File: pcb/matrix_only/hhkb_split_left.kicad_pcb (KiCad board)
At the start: 2 copper layers, 138.4 x 97.4 mm, 65 parts, among them SW1 CPG151101S11-2, SW10 CPG151101S11-2, SW11 CPG151101S11-2, SW12 CPG151101S11-2, SW13 CPG151101S11-2, SW14 CPG151101S11-2, SW15 CPG151101S11-2, SW16 CPG151101S11-2, SW17 CPG151101S11-2, SW18 CPG151101S11-2, SW19 CPG151101S11-2, SW2 CPG151101S11-2, SW20 CPG151101S11-2, SW21 CPG151101S11-2, SW22 CPG151101S11-2, SW23 CPG151101S11-2, SW24 CPG151101S11-2, SW25 CPG151101S11-2, SW26 CPG151101S11-2, SW27 CPG151101S11-2, SW3 CPG151101S11-2, SW4 CPG151101S11-2, SW5 CPG151101S11-2, SW6 CPG151101S11-2, SW7 CPG151101S11-2, SW8 CPG151101S11-2, SW9 CPG151101S11-2, U1 74LVC595

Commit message: #19 決着: 右 J_DB を 1.63mm 手前へ（ソケットまで 3.9mm）、左右の配線と露出ビアを利用者が引き直し。3 基板とも DRC 0 / 未配線 0
- 右: MP パッドに当たった COL0 の迂回、V3V3 の裏面残骸 2 本を削除、MOSI ビアを 0.15mm 移動、混んだ V3V3 ビアを φ0.56（アニュラー 0.13）
- gen_pcb: 右 J_DB の dy を +1.235（中心 y=88.46）に
- 検査 458 緑・赤 1（左 SPI_SCK の露出のみ・任意）
- 記録・部品記録・DRC 記録・証拠ページを更新

Co-Authored-By: Claude Fable 5 <noreply@anthropic.com>
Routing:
- net SPARE: track 9.81 -> 14.7 mm
- net SPARE2: track 10.2 -> 13.0 mm
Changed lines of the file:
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@@
 	)
 	(via
-		(at 209.94 75.69)
+		(at 216.34 77.01)
 		(size 0.6)
 		(drill 0.3)
@@
 	)
 	(segment
-		(start 209.93 78.36)
+		(start 209.93 77.32)
 		(end 209.93 83.964314)
+		(width 0.2)
+		(layer "B.Cu")
+		(net "SPARE")
+	)
+	(segment
+		(start 216.34 77.01)
+		(end 210.24 77.01)
 		(width 0.2)
 		(layer "B.Cu")
@@
 	)
 	(segment
-		(start 209.94 75.69)
-		(end 209.94 78.35)
-		(width 0.2)
-		(layer "B.Cu")
-		(net "SPARE")
-	)
-	(segment
-		(start 209.94 78.35)
-		(end 209.93 78.36)
-		(width 0.2)
-		(layer "B.Cu")
-		(net "SPARE")
-	)
-	(segment
 		(start 209.63125 84.263064)
 		(end 209.63125 85.375)
@@
 		(net "SPARE")
 	)
+	(segment
+		(start 210.24 77.01)
+		(end 209.93 77.32)
+		(width 0.2)
+		(layer "B.Cu")
+		(net "SPARE")
+	)
 	(via
-		(at 211.22 75.67)
+		(at 216.36 78.23)
 		(size 0.6)
 		(drill 0.3)
@@
 	)
 	(segment
-		(start 211.22 75.67)
-		(end 210.53 76.36)
-		(width 0.2)
-		(layer "B.Cu")
-		(net "SPARE2")
-	)
-	(segment
 		(start 210.13125 84.32875)
 		(end 210.13125 85.375)
@@
 	)
 	(segment
-		(start 210.53 76.36)
+		(start 216.36 78.23)
+		(end 210.76 78.23)
+		(width 0.2)
+		(layer "B.Cu")
+		(net "SPARE2")
+	)
+	(segment
+		(start 210.53 78.46)
 		(end 210.53 83.93)
 		(width 0.2)
 		(layer "B.Cu")
+		(net "SPARE2")
+	)
+	(segment
+		(start 210.76 78.23)
+		(end 210.53 78.46)
+		(width 0.2)
+		(layer "B.Cu")

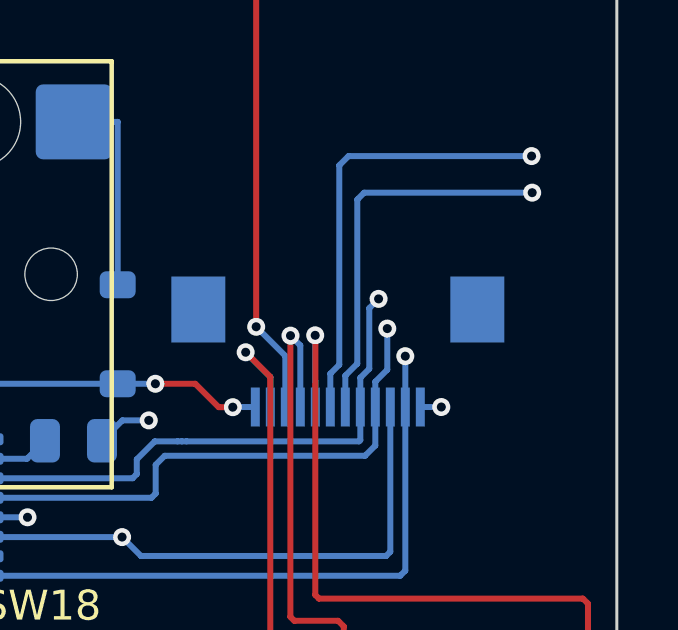
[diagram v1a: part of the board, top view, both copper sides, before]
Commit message: #49 左の SCK・CS・V3V3 にも露出ビア（利用者）。露出は左右の全ネットがビアに。3 基板 DRC 0・検査 460 緑
Co-Authored-By: Claude Fable 5 <noreply@anthropic.com>
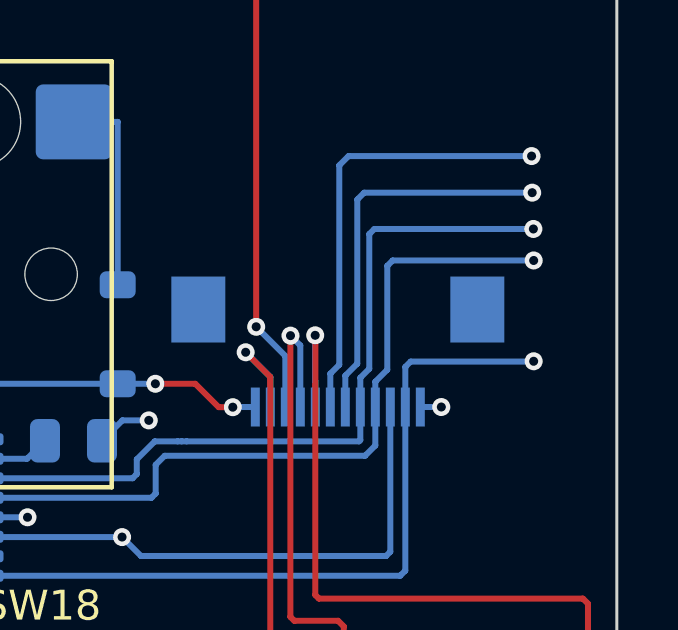
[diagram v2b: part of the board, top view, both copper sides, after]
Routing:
- net SPI_SCK: track 18.4 -> 26.0 mm
- net CS: track 18.6 -> 25.5 mm
- net V3V3: track 31.9 -> 36.0 mm
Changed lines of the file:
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@@
 	)
 	(via
-		(at 211.24 81.77)
+		(at 216.4 79.44)
 		(size 0.6)
 		(drill 0.3)
@@
 	)
 	(segment
-		(start 210.63125 85.375)
-		(end 210.63125 84.39875)
-		(width 0.2)
-		(layer "B.Cu")
-		(net "SPI_SCK")
-	)
-	(segment
 		(start 204.68 86.52)
 		(end 204.54 86.52)
@@
 	)
 	(segment
+		(start 210.93 79.61)
+		(end 210.93 84.1)
+		(width 0.2)
+		(layer "B.Cu")
+		(net "SPI_SCK")
+	)
+	(segment
 		(start 210.6312 85.375)
 		(end 210.6312 86.4788)
@@
 	)
 	(segment
-		(start 210.63125 84.39875)
-		(end 210.93 84.1)
+		(start 210.93 84.1)
+		(end 210.63125 84.39875)
 		(width 0.2)
 		(layer "B.Cu")
@@
 	)
 	(segment
-		(start 210.93 84.1)
-		(end 210.93 82.08)
+		(start 216.4 79.44)
+		(end 211.1 79.44)
 		(width 0.2)
 		(layer "B.Cu")
@@
 	)
 	(segment
-		(start 210.93 82.08)
-		(end 211.24 81.77)
+		(start 211.1 79.44)
+		(end 210.93 79.61)
+		(width 0.2)
+		(layer "B.Cu")
+		(net "SPI_SCK")
+	)
+	(segment
+		(start 210.63125 84.39875)
+		(end 210.63125 85.375)
 		(width 0.2)
 		(layer "B.Cu")
@@
 	)
 	(via
-		(at 211.53 82.76)
+		(at 216.41 80.49)
 		(size 0.6)
 		(drill 0.3)
@@
 	)
 	(segment
+		(start 211.53 84.131471)
+		(end 211.13125 84.530221)
+		(width 0.2)
+		(layer "B.Cu")
+		(net "CS")
+	)
+	(segment
 		(start 210.79 87)
 		(end 211.1312 86.6587)
@@
 	)
 	(segment
-		(start 211.13125 84.530221)
-		(end 211.53 84.131471)
-		(width 0.2)
-		(layer "B.Cu")
-		(net "CS")
-	)
-	(segment
 		(start 204.11 87)
 		(end 210.79 87)
@@
 	)
 	(segment
-		(start 211.53 82.76)
-		(end 211.68 82.76)
-		(width 0.2)
-		(layer "B.Cu")
-		(net "CS")
-	)
-	(segment
-		(start 211.53 84.131471)
-		(end 211.53 82.76)
+		(start 211.13125 84.530221)
+		(end 211.13125 85.375)
 		(width 0.2)
 		(layer "B.Cu")
@@
 	)
 	(segment
+		(start 211.53 80.67)
+		(end 211.53 84.131471)
+		(width 0.2)
+		(layer "B.Cu")
+		(net "CS")
+	)
+	(segment
+		(start 211.71 80.49)
+		(end 211.53 80.67)
+		(width 0.2)
+		(layer "B.Cu")
+		(net "CS")
+	)
+	(segment
+		(start 216.41 80.49)
+		(end 211.71 80.49)
+		(width 0.2)
+		(layer "B.Cu")
+		(net "CS")
+	)
+	(segment
 		(start 211.1312 86.6587)
 		(end 211.1312 85.375)
@@
 		(start 203.81 88.26)
 		(end 203.81 87.3)
-		(width 0.2)
-		(layer "B.Cu")
-		(net "CS")
-	)
-	(segment
-		(start 211.13125 85.375)
-		(end 211.13125 84.530221)
 		(width 0.2)
 		(layer "B.Cu")
@@
 	)
 	(via
-		(at 212.13 83.68)
+		(at 216.41 83.85)
 		(size 0.6)
 		(drill 0.3)
@@
 	)
 	(segment
+		(start 216.41 83.85)
+		(end 216.4 83.86)
+		(width 0.2)
+		(layer "B.Cu")
+		(net "V3V3")
+	)
+	(segment
 		(start 195.9 87.1)
 		(end 195.77 87.23)
@@
 	)
 	(segment
-		(start 212.13125 85.375)
-		(end 212.13125 83.68125)
+		(start 212.13125 84.03875)
+		(end 212.31 83.86)
 		(width 0.2)
 		(layer "B.Cu")
@@
 	)
 	(segment
+		(start 212.13125 85.375)
+		(end 212.13125 84.03875)
+		(width 0.2)
+		(layer "B.Cu")
+		(net "V3V3")
+	)
+	(segment
 		(start 212.1312 90.8287)
 		(end 211.96 91)
@@
 	)
 	(segment
+		(start 216.4 83.86)
+		(end 212.31 83.86)
+		(width 0.2)
+		(layer "B.Cu")
+		(net "V3V3")
+	)
+	(segment
 		(start 198 87.1)
 		(end 195.9 87.1)
@@
 		(width 0.2)
 		(layer "B.Cu")
+		(net "V3V3")
+	)
+	(segment
+		(start 212.13125 85.375)
+		(end 212.15 85.35625)
+		(width 0.2)
+		(layer "B.Cu")

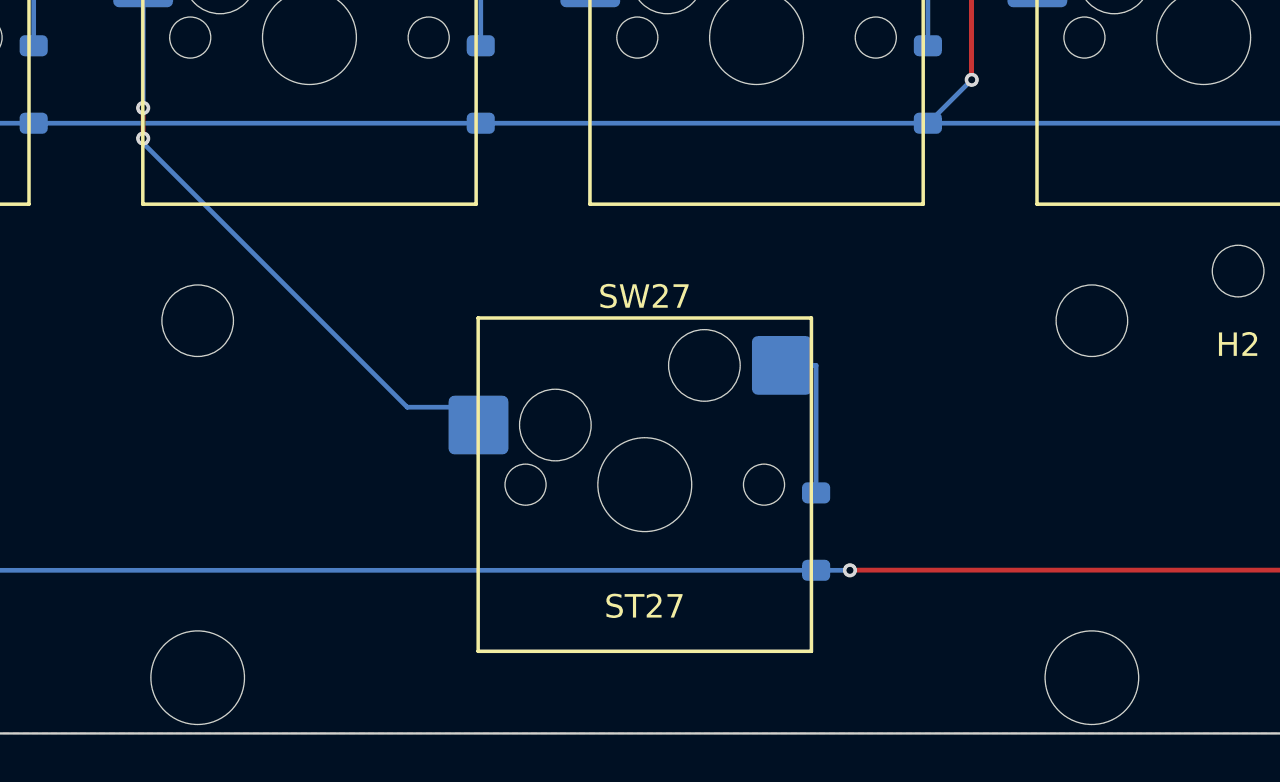
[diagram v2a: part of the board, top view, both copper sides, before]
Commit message: スペースキー 2.75u 化を基板まで反映（3 基板とも DRC 0 / 未配線 0）
設計側（29f4471）に続き、基板を作り直した。

**matrix_only のスペースキーを 2.75u へ**（KiCad の API で差し替え）:
- SW27/SW32 → SW_Hotswap_Kailh_MX_2.75u
- ST27/ST32 → Stabilizer_Cherry_MX_2.00u（穴が ±19.05 → ±11.938）
- SW/ST/D を x 左 −2.38125 / 右 +2.38125 だけ移動

**配線**: ダイオード側 2 本ずつは平行移動で端点がパッドに 0.0001mm 一致。
COL は経路の形が変わるので引き直した（左 COL3・右 COL0）。
⚠️ **利用者の指摘「col0 の配線が規則的じゃない」「col3 も」で 1 度やり直した。**
最初はクリアランスだけ見て 71.9°/2.6°/28.1°/82.9° の半端な角度で引いており、
**この板の他の配線は全部 0°/45°/90°/135°** だった。
縦→45°→水平の 3 区間に作り直し、角度を 45° の倍数に固定したまま
総当たりで障害物との距離が最大の経路を選んだ（左 +0.656mm / 右 +1.650mm）。

**シルクが 0.12mm のまま残っていたのも直した**（gen_pcb の仕上げを
通らないため。→ pcb-routing-handover.md に落とし穴として記録）。

検証: 3 基板とも 違反 0 / 未配線 0。スタビ 4 個すべて ±11.938。
STL のハウジング間隔を実測して 23.880mm（=2u）を確認。
fab_check（595 48 パッド / XIAO 14 パッド / 61 キー経路）全 OK。
基板の外形は不変（左 138.363×97.4 / 右 171.70×97.4 / 子 21.0×32.0）。
検査 464 緑。

記録: スタビの節を 2.75u 前提に書き直し、国内入手性の調査結果
（2u は潤沢・3u は買えない）と、FFC コネクタ C88360 の在庫が
40 日で 0 になるペースであることを追記。#46 の古い「次の一手」も直した。

Co-Authored-By: Claude Opus 5 (1M context) <noreply@anthropic.com>
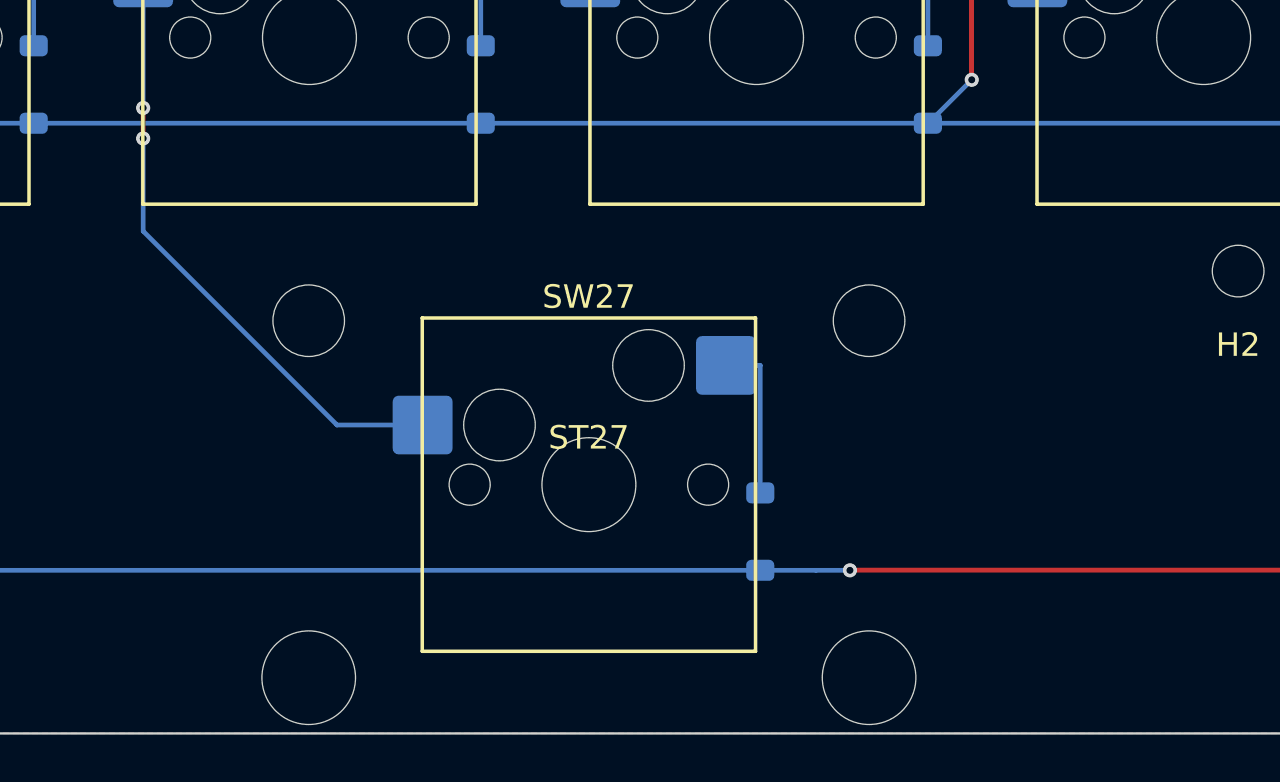
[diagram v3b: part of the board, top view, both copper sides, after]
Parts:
- ST27: value Stabilizer_Cherry_MX_3.00u -> Stabilizer_Cherry_MX_2.00u; footprint Stabilizer_Cherry_MX_3.00u -> Stabilizer_Cherry_MX_2.00u
- SW27: footprint SW_Hotswap_Kailh_MX_3.00u -> SW_Hotswap_Kailh_MX_2.75u
- moved D27 2.38 mm to (190.6, 140.1)
- moved ST27 2.38 mm to (183.3, 138.1)
- moved SW27 2.38 mm to (183.3, 138.1)
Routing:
- net COL3: track 136.0 -> 135.3 mm

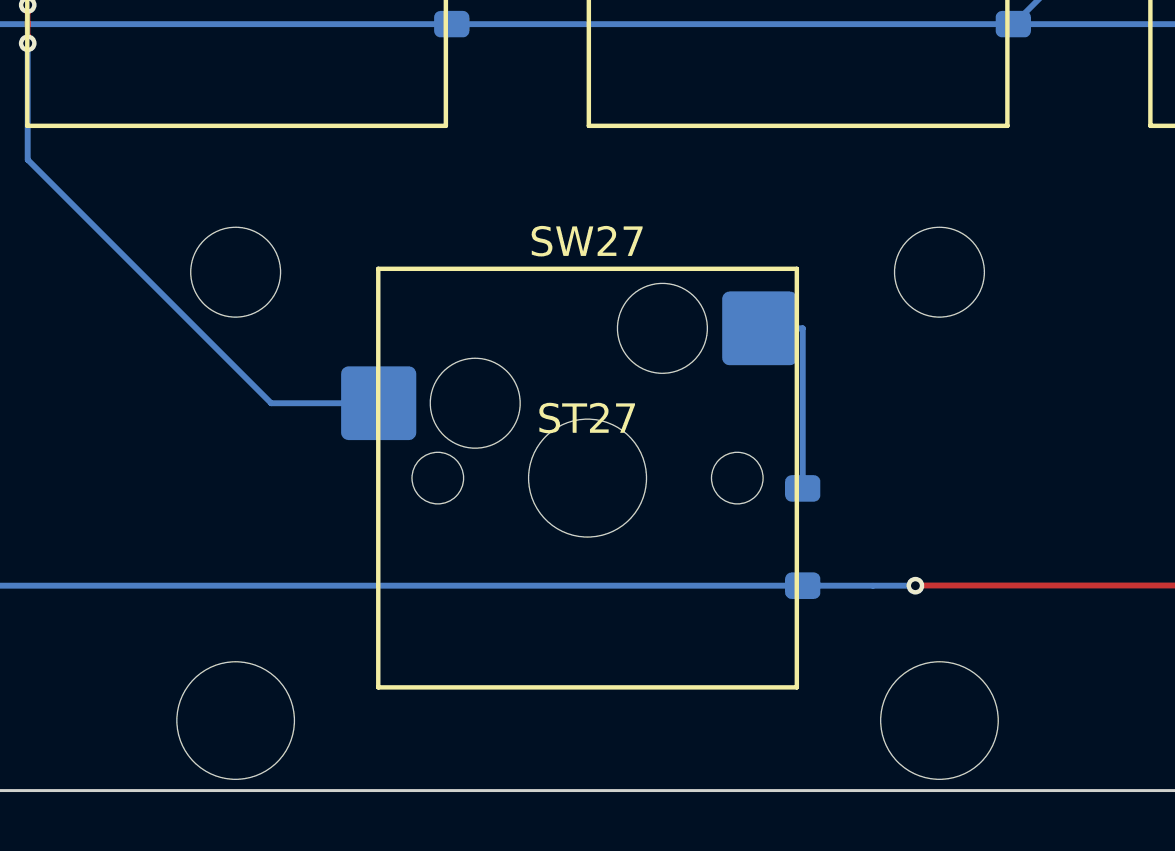
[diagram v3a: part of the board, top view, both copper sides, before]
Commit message: #53 決着: スペースのスタビ 2 個を 180°（ワイヤ奥）に回す。大穴が板前縁まで 0.381mm だったのが小穴 2.14mm に。interface.stab_flipped を gen_pcb・gen_plate・find_mounts が見る。matrix_only の ST27/ST32 を回して手順どおり再生成、3 基板 DRC 0・警告数不変。NPTH の縁 ≥1.0mm の検査を足し、回す前の板で 0.381 を検出することを確認。実形状のスタビ開口検査・test_assembly 69 件・高速 387 件緑
Co-Authored-By: Claude Fable 5 <noreply@anthropic.com>
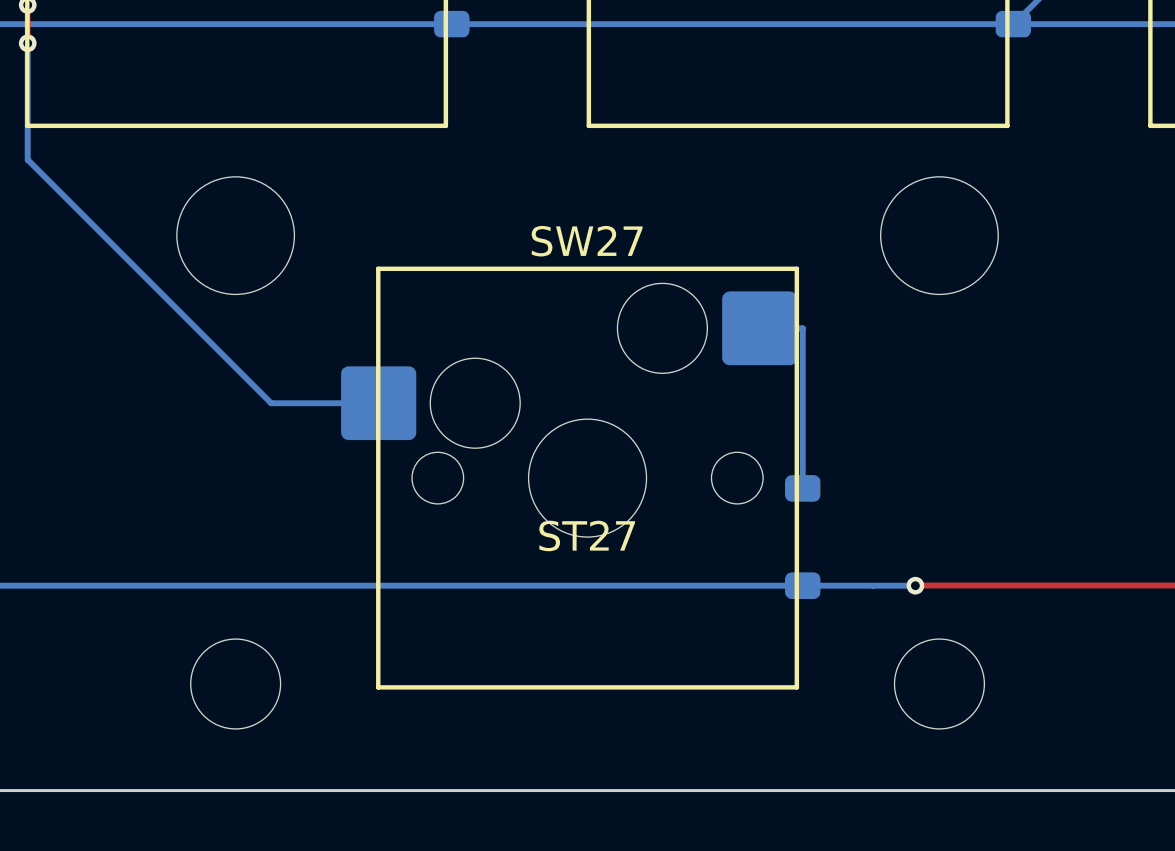
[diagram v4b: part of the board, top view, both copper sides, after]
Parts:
- turned ST27 to 180 degrees
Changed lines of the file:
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@@
 	(footprint "Stabilizer_Cherry_MX_2.00u"
 		(layer "F.Cu")
-		(at 183.3375 138.1)
+		(at 183.3375 138.1 180)
 		(descr "Cherry MX PCB Stabilizer 2.00u 2.25u 2.50u 2.75u")
 		(tags "Cherry MX Keyboard Stabilizer 2.00u 2.25u 2.50u 2.75u Cutout")
 		(property "Reference" "ST27"
-			(at 0 -2 0)
+			(at 0 -2 180)
 			(layer "F.SilkS")
 			(effects
@@
 		)
 		(property "Value" "Stabilizer_Cherry_MX_2.00u"
-			(at 0 2 0)
+			(at 0 2 180)
 			(layer "F.Fab")
 			(effects
@@
 		)
 		(property "Datasheet" ""
-			(at 0 0 0)
+			(at 0 0 180)
 			(layer "F.Fab")
 			(hide yes)
@@
 		)
 		(property "Description" ""
-			(at 0 0 0)
+			(at 0 0 180)
 			(layer "F.Fab")
 			(hide yes)
@@
 		(duplicate_pad_numbers_are_jumpers no)
 		(fp_line
+			(start 0 2)
+			(end 0 -2)
+			(stroke
+				(width 0.1)
+				(type solid)
+			)
+			(layer "Dwgs.User")
+		)
+		(fp_line
 			(start -2 0)
 			(end 2 0)
@@
 		)
 		(fp_line
-			(start 0 2)
-			(end 0 -2)
+			(start 15.313 6.77)
+			(end 15.313 -5.53)
 			(stroke
 				(width 0.1)
 				(type solid)
 			)
-			(layer "Dwgs.User")
+			(layer "Eco1.User")
 		)
 		(fp_line
-			(start -15.313 -5.53)
-			(end -15.313 6.77)
+			(start 15.313 -5.53)
+			(end 8.563 -5.53)
+			(stroke
+				(width 0.1)
+				(type solid)
+			)
+			(layer "Eco1.User")
+		)
+		(fp_line
+			(start 8.563 6.77)
+			(end 15.313 6.77)
+			(stroke
+				(width 0.1)
+				(type solid)
+			)
+			(layer "Eco1.User")
+		)
+		(fp_line
+			(start 8.563 -5.53)
+			(end 8.563 6.77)
+			(stroke
+				(width 0.1)
+				(type solid)
+			)
+			(layer "Eco1.User")
+		)
+		(fp_line
+			(start -8.563 6.77)
+			(end -8.563 -5.53)
+			(stroke
+				(width 0.1)
+				(type solid)
+			)
+			(layer "Eco1.User")
+		)
+		(fp_line
+			(start -8.563 -5.53)
+			(end -15.313 -5.53)
 			(stroke
 				(width 0.1)
@@
 		)
 		(fp_line
-			(start -8.563 -5.53)
-			(end -15.313 -5.53)
-			(stroke
-				(width 0.1)
-				(type solid)
-			)
-			(layer "Eco1.User")
-		)
-		(fp_line
-			(start -8.563 6.77)
-			(end -8.563 -5.53)
-			(stroke
-				(width 0.1)
-				(type solid)
-			)
-			(layer "Eco1.User")
-		)
-		(fp_line
-			(start 8.563 -5.53)
-			(end 8.563 6.77)
-			(stroke
-				(width 0.1)
-				(type solid)
-			)
-			(layer "Eco1.User")
-		)
-		(fp_line
-			(start 8.563 6.77)
-			(end 15.313 6.77)
-			(stroke
-				(width 0.1)
-				(type solid)
-			)
-			(layer "Eco1.User")
-		)
-		(fp_line
-			(start 15.313 -5.53)
-			(end 8.563 -5.53)
-			(stroke
-				(width 0.1)
-				(type solid)
-			)
-			(layer "Eco1.User")
-		)
-		(fp_line
-			(start 15.313 6.77)
-			(end 15.313 -5.53)
+			(start -15.313 -5.53)
+			(end -15.313 6.77)
 			(stroke
 				(width 0.1)
@@
 		)
 		(fp_text user "${REFERENCE}"
-			(at 0 0 0)
+			(at 0 0 180)
 			(layer "F.Fab")
 			(effects
@@
 		)
 		(pad "" np_thru_hole circle
-			(at -11.938 -6.985)
+			(at -11.938 -6.985 180)
 			(size 3.048 3.048)
 			(drill 3.048)
@@
 		)
 		(pad "" np_thru_hole circle
-			(at -11.938 8.225)
+			(at -11.938 8.225 180)
 			(size 3.9878 3.9878)
 			(drill 3.9878)
@@
 		)
 		(pad "" np_thru_hole circle
-			(at 11.938 -6.985)
+			(at 11.938 -6.985 180)
 			(size 3.048 3.048)
 			(drill 3.048)
@@
 		)
 		(pad "" np_thru_hole circle
-			(at 11.938 8.225)
+			(at 11.938 8.225 180)
 			(size 3.9878 3.9878)
 			(drill 3.9878)
